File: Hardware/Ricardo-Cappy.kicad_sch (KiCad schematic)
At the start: 4 parts, among them J3 Conn_02x20_Odd_Even

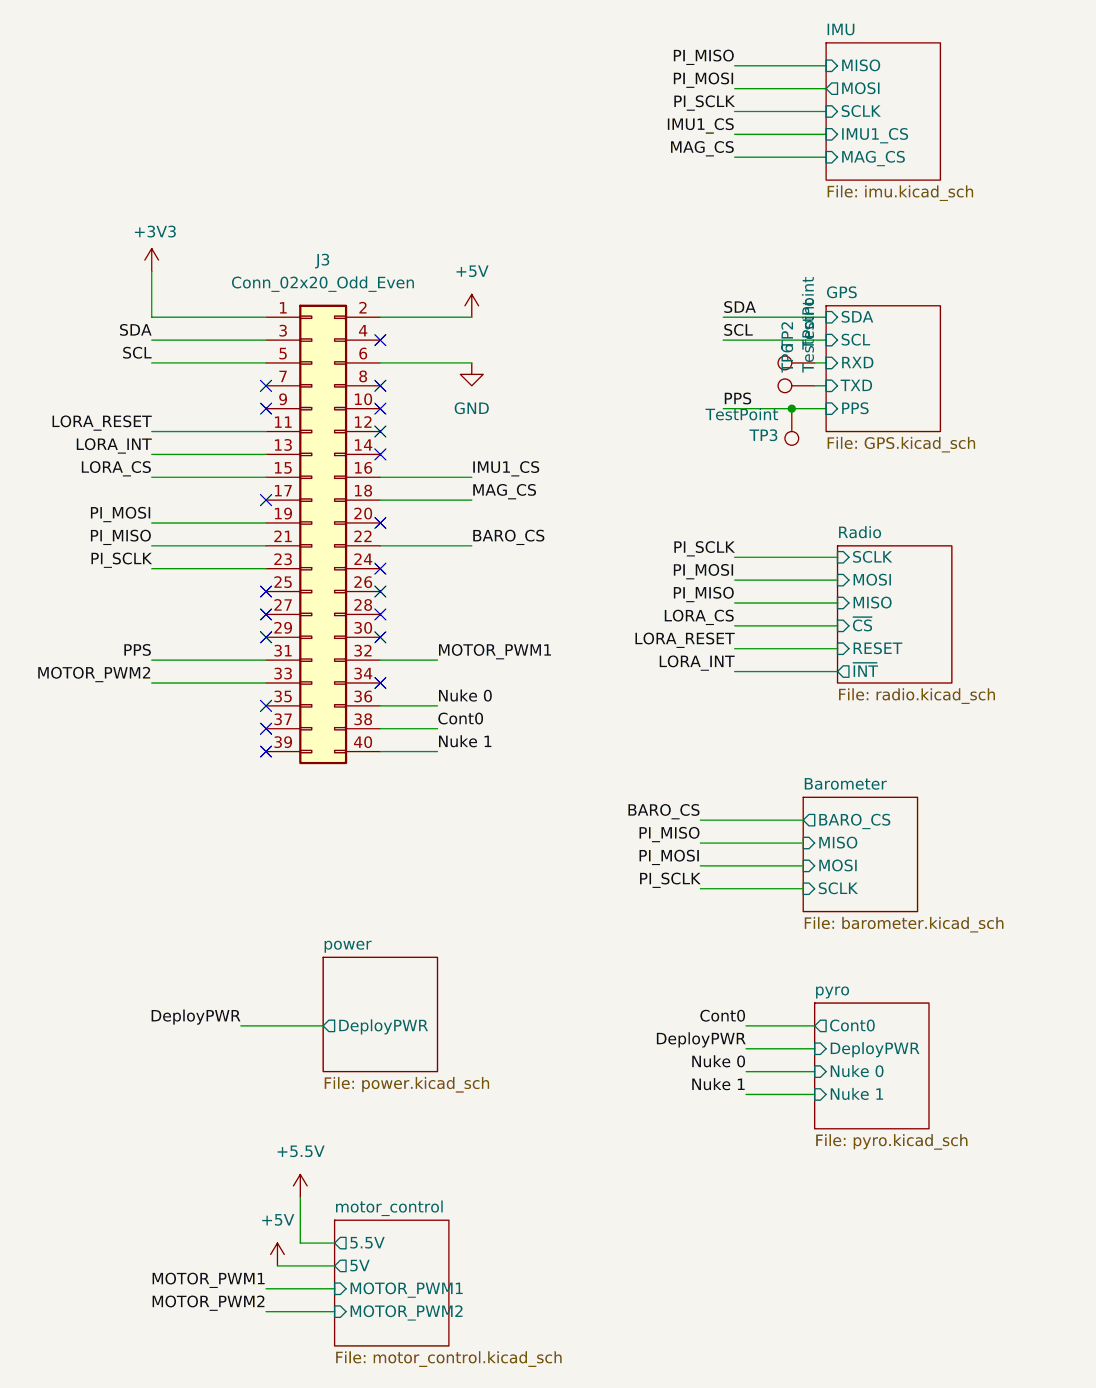
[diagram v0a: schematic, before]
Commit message: Modified power
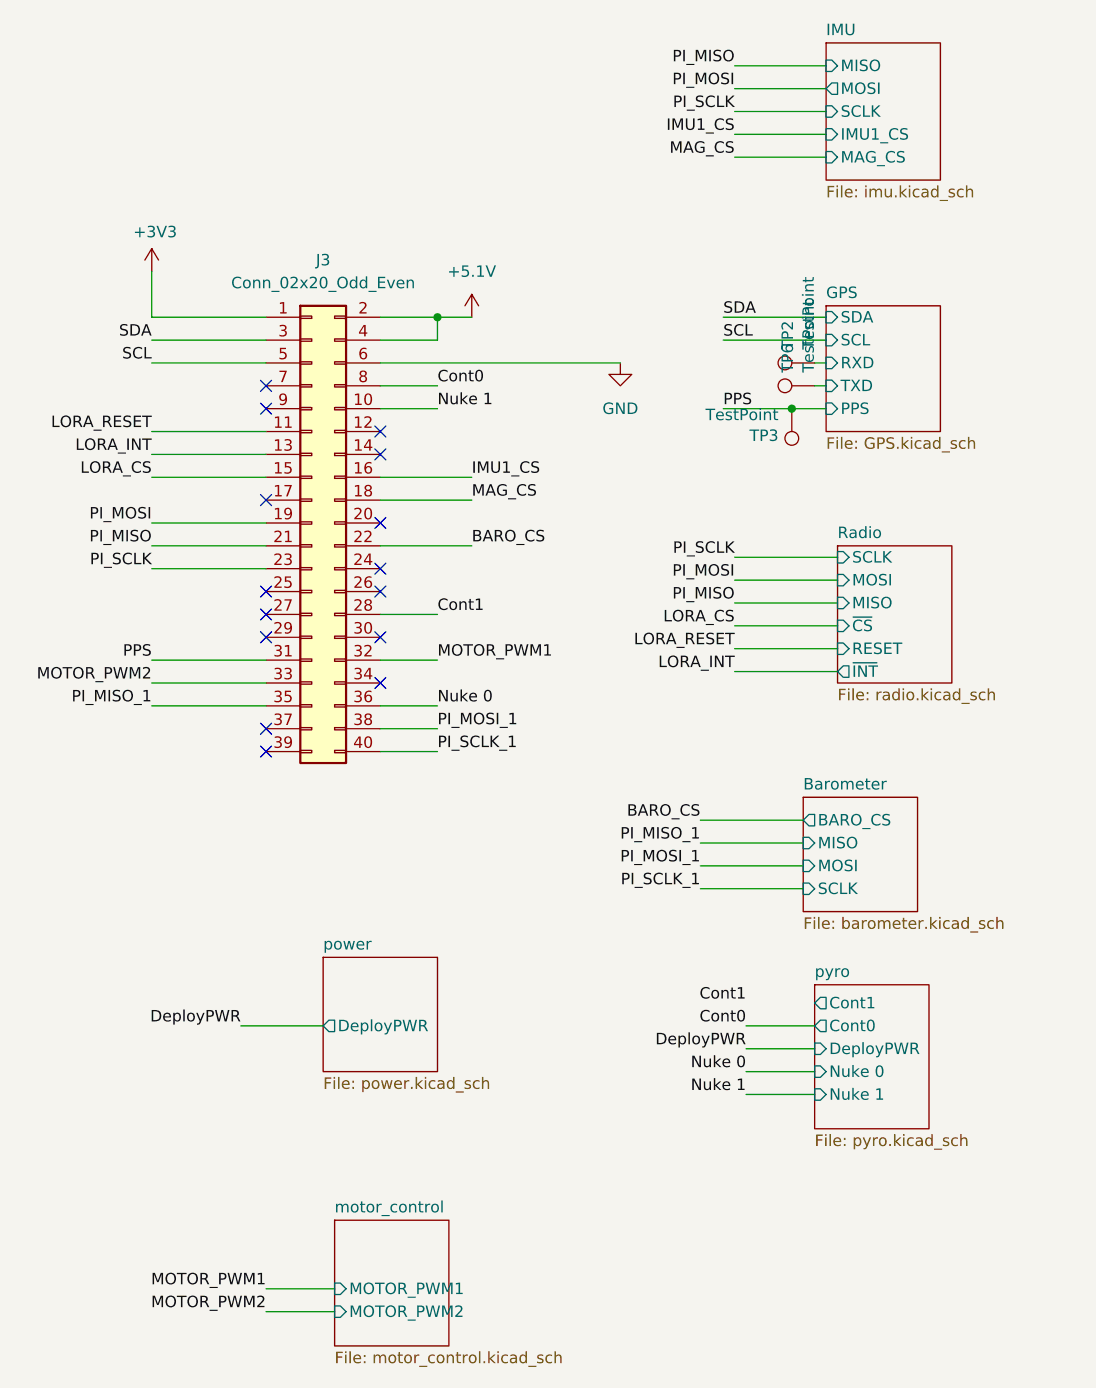
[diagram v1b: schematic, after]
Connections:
- net +5V is gone; now on net +5.1V: J3.2 (Pin_2)
- net Cont0: now also J3.8 (Pin_8); no longer J3.38 (Pin_38)
- net Nuke 1: now also J3.10 (Pin_10); no longer J3.40 (Pin_40)
- net Cont1: now reaches J3.28 (Pin_28)
- net PI_MISO_1: now reaches J3.35 (Pin_35)
- net +5.1V: now reaches J3.4 (Pin_4)
- new net PI_MOSI_1: J3.38 (Pin_38)
- new net PI_SCLK_1: J3.40 (Pin_40)
- no-connect marks 20 -> 15
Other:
- sheet motor_control ports: added none; removed 5.5V, 5V
- sheet pyro ports: added Cont1; removed none

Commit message: Fixed power
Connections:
- net GND: now also J3.14 (Pin_14), J3.20 (Pin_20), J3.25 (Pin_25), J3.30 (Pin_30), J3.34 (Pin_34), J3.39 (Pin_39), J3.9 (Pin_9)
- no-connect marks 15 -> 8

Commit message: Corrected accidentally deleted connection, reorganised PCB layout (still very WIP)
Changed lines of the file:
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@@
+	(wire
+		(pts
+			(xy 149.86 124.46) (xy 157.48 124.46)
+		)
+		(stroke
+			(width 0)
+			(type default)
+		)
+	)
 	(wire
 		(pts
